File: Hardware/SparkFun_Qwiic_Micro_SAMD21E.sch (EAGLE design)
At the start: 40 parts, among them Q1 2.5A/30V/105mΩ, U1 3.3V, U2 W25Q32FV

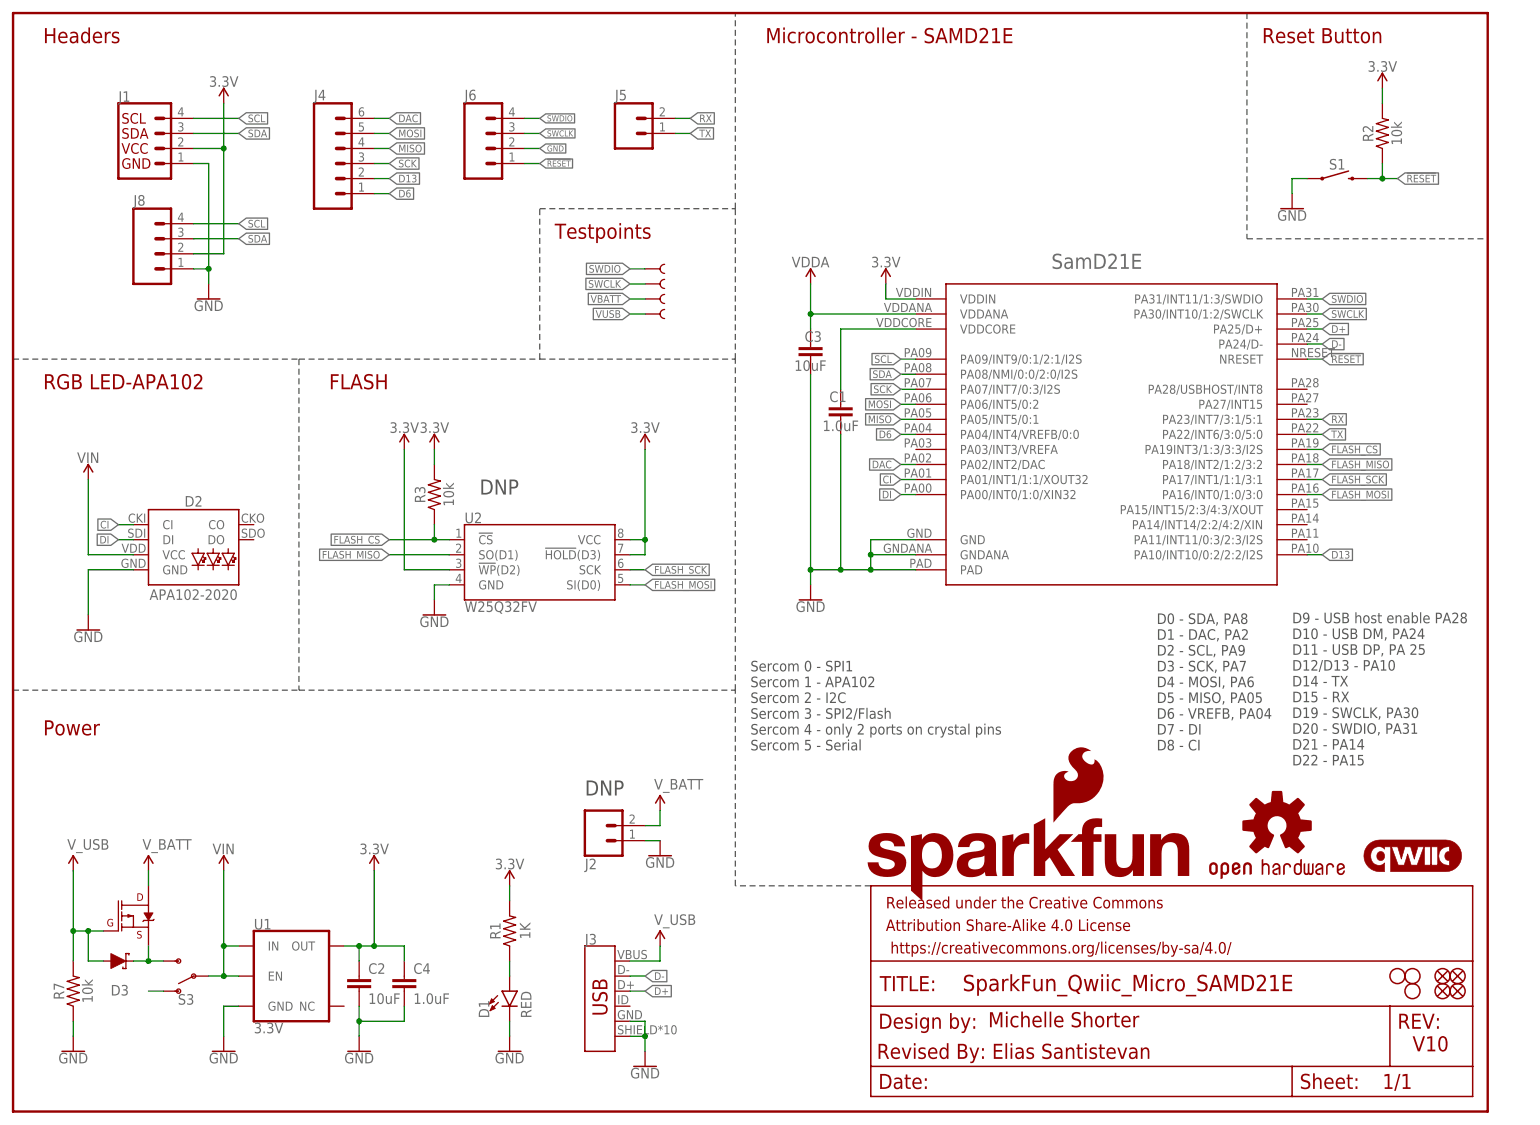
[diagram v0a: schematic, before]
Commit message: Improves all silk, replaces 0603 resistor with 0402, updates trace work for better ground pour
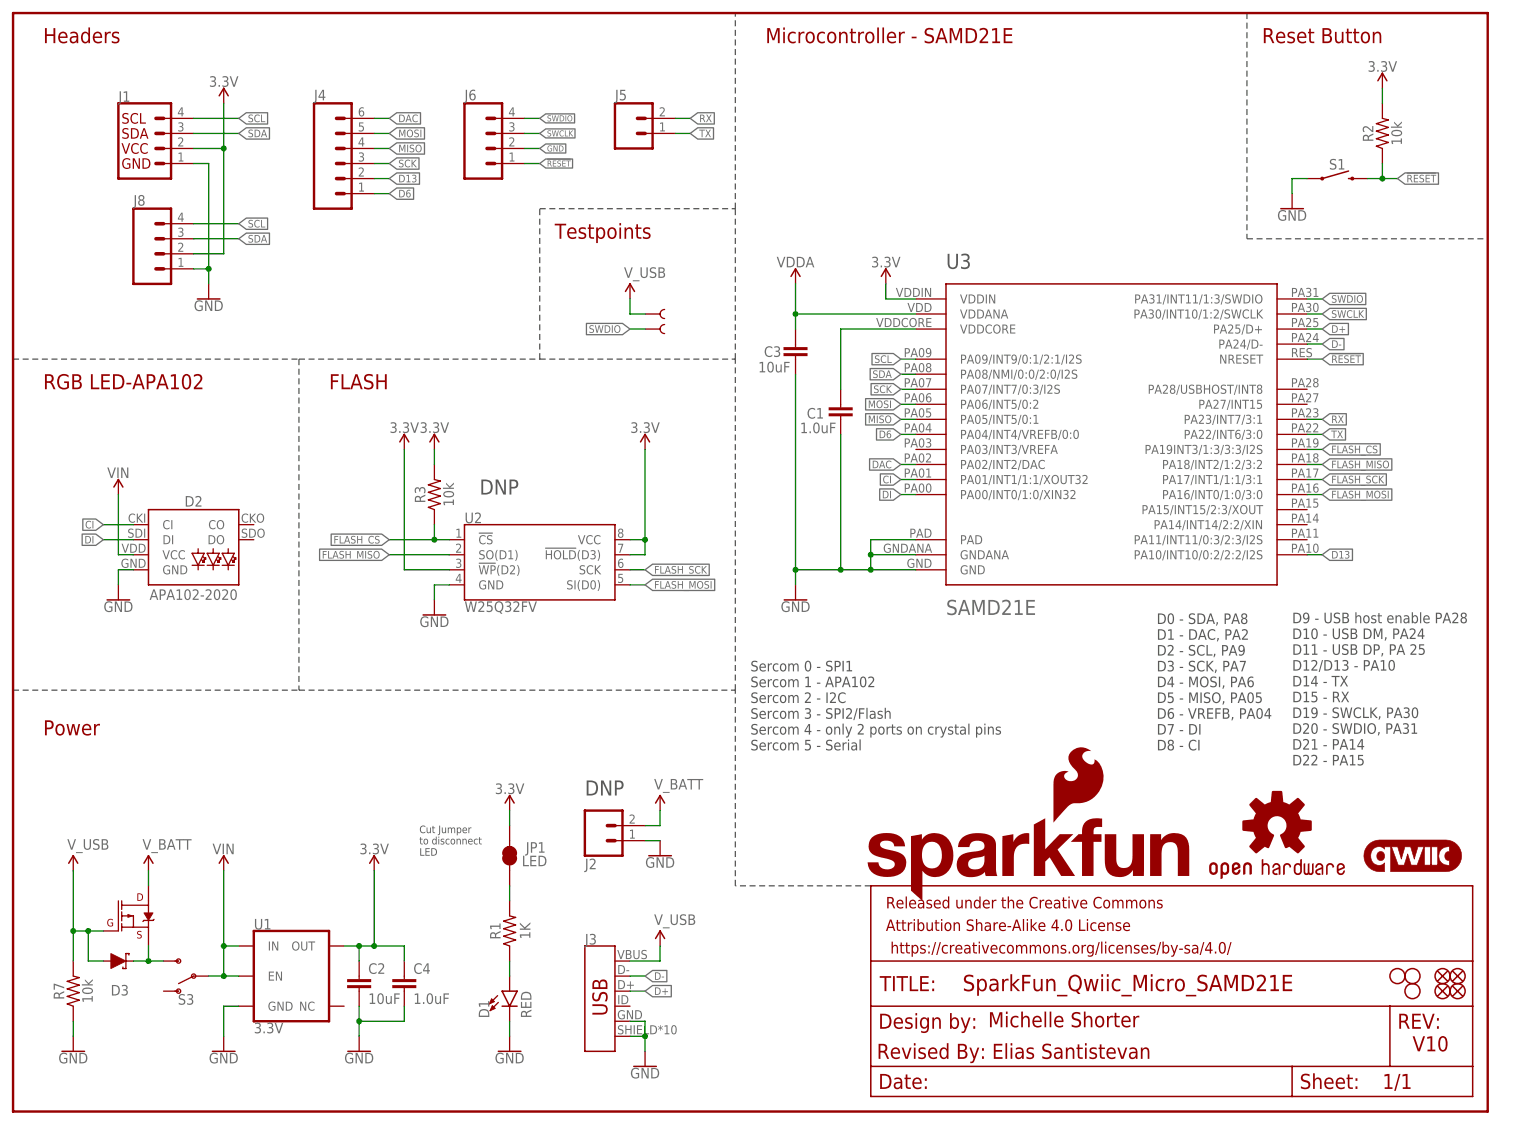
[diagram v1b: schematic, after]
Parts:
- removed SAMD21E18: SAMD32E, Test:SAMD32E
- removed TP2, TP4: TEST-POINTTP_15TH_THRU, SparkFun-Connectors:TEST-POINTTP_15TH_THRU
- added JP1: LED, SparkFun-Jumpers:JUMPER-SMT_2_NC_TRACE_SILK
- added U3: SAMD21E, Test:SAMD21E
- J6: device SparkFun-Connectors:CONN_041.27MM -> SparkFun-Connectors:CONN_041.27MM_NO_SILK
- Q1: value 2.5A/30V/105mΩ -> 3.1A/30V/105mΩ
- R7: device SparkFun-Resistors:10KOHM-0603-1/10W-1% -> SparkFun-Resistors:10KOHM-0402-1/16W-1%
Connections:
- removed net N$1 (its old number): S3.O
- removed net VBATT: Q1.D, TP2.1
- removed net VUSB: D3.A, Q1.G, R7.2, TP1.1
- new net N$2: JP1.1, R1.2
- net !RESET: now also U3.NRESET; no longer SAMD21E18.NRESET
- net 3.3V: now also JP1.2, U3.VDDIN; no longer R1.2, SAMD21E18.VDDIN
- net CI: now also U3.PA01/INT1/1:1/XOUT32; no longer SAMD21E18.PA01/INT1/1:1/XOUT32
- net D+: now also U3.PA25/D+; no longer SAMD21E18.PA25/D+
- net D-: now also U3.PA24/D-; no longer SAMD21E18.PA24/D-
- net D13: now also U3.PA10/INT10/0:2/2:2/I2S; no longer SAMD21E18.PA10/INT10/0:2/2:2/I2S
- net D6: now also U3.PA04/INT4/VREFB/0:0; no longer SAMD21E18.PA04/INT4/VREFB/0:0
- net DAC: now also U3.PA02/INT2/DAC; no longer SAMD21E18.PA02/INT2/DAC
- net DI: now also U3.PA00/INT0/1:0/XIN32; no longer SAMD21E18.PA00/INT0/1:0/XIN32
- net FLASH_CS: now also U3.PA19INT3/1:3/3:3/I2S; no longer SAMD21E18.PA19INT3/1:3/3:3/I2S
- net FLASH_MISO: now also U3.PA18/INT2/1:2/3:2; no longer SAMD21E18.PA18/INT2/1:2/3:2
- net FLASH_MOSI: now also U3.PA16/INT0/1:0/3:0; no longer SAMD21E18.PA16/INT0/1:0/3:0
- net FLASH_SCK: now also U3.PA17/INT1/1:1/3:1; no longer SAMD21E18.PA17/INT1/1:1/3:1
- net GND: now also U3.GND, U3.GNDANA, U3.PAD; no longer SAMD21E18.GND, SAMD21E18.GNDANA, SAMD21E18.PAD
- net MISO: now also U3.PA05/INT5/0:1; no longer SAMD21E18.PA05/INT5/0:1
- net MOSI: now also U3.PA06/INT5/0:2; no longer SAMD21E18.PA06/INT5/0:2
- net RX: now also U3.PA23/INT7/3:1; no longer SAMD21E18.PA23/INT7/3:1/5:1
- net SCK: now also U3.PA07/INT7/0:3/I2S; no longer SAMD21E18.PA07/INT7/0:3/I2S
- net SCL: now also U3.PA09/INT9/0:1/2:1/I2S; no longer SAMD21E18.PA09/INT9/0:1/2:1/I2S
- net SDA: now also U3.PA08/NMI/0:0/2:0/I2S; no longer SAMD21E18.PA08/NMI/0:0/2:0/I2S
- net SWCLK: now also U3.PA30/INT10/1:2/SWCLK; no longer SAMD21E18.PA30/INT10/1:2/SWCLK, TP4.1
- net SWDIO: now also U3.PA31/INT11/1:3/SWDIO; no longer SAMD21E18.PA31/INT11/1:3/SWDIO
- net TX: now also U3.PA22/INT6/3:0; no longer SAMD21E18.PA22/INT6/3:0/5:0
- net VDDA: now also U3.VDDANA; no longer SAMD21E18.VDDANA
- net VDDCORE: now also U3.VDDCORE; no longer SAMD21E18.VDDCORE
- net V_BATT: now also Q1.D
- net V_USB: now also D3.A, Q1.G, R7.2, TP1.1
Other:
- note added: "Cut Jumper to disconnect LED"
- note added: "U3"
- moved on the sheet: C3

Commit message: Moves some traces
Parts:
- LOGO3: value SFE_LOGO_FLAME.1_INCH -> SFE_LOGO_FLAME.2_INCH; device SparkFun-Aesthetics:SFE_LOGO_FLAME.1_INCH -> SparkFun-Aesthetics:SFE_LOGO_FLAME.2_INCH
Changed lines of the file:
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@@
 <part name="FRAME1" library="SparkFun-Aesthetics" deviceset="FRAME-LETTER" device=""/>
 <part name="LOGO1" library="SparkFun-Aesthetics" deviceset="OSHW-LOGO" device="S"/>
-<part name="LOGO3" library="SparkFun-Aesthetics" deviceset="SFE_LOGO_FLAME" device=".1_INCH"/>
+<part name="LOGO3" library="SparkFun-Aesthetics" deviceset="SFE_LOGO_FLAME" device=".2_INCH" value="SFE_LOGO_FLAME.2_INCH"/>
 <part name="H1" library="SparkFun-Hardware" deviceset="STAND-OFF" device=""/>
 <part name="H2" library="SparkFun-Hardware" deviceset="STAND-OFF" device=""/>

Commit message: Updates micro-controller symbol with Arduino digital pin assignments
* replaces lipo battery symbol with better one
* Re-adds battery line test ponit
* Removes info text about Arduino pin assignments
* Improves notes on SERCOM ports
* Re-numbers all parts
* Removes test library - no longer needed.
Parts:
- removed J8: (no value), SparkFun-Connectors:CONN_041X04_NO_SILK
- removed R7: 10k, SparkFun-Resistors:10KOHM-0402-1/16W-1%
- removed S3: (no value), SparkFun-Switches:SWITCH-SPDT-SMD-RIGHT-ANGLE
- added J7: (no value), SparkFun-Connectors:CONN_021X02_NO_SILK
- added R4: 10k, SparkFun-Resistors:10KOHM-0402-1/16W-1%
- added S2: MOMENTARY-SWITCH-SPST-SMD-4.6X2.8MM, SparkFun-Switches:MOMENTARY-SWITCH-SPST-SMD-4.6X2.8MM
- added TP2: TEST-POINTTP_15TH_THRU, SparkFun-Connectors:TEST-POINTTP_15TH_THRU
- C1: value 1.0uF -> 10uF; device SparkFun-Capacitors:1.0UF-0402-16V-10% -> SparkFun-Capacitors:10UF-0603-6.3V-20%
- C2: value 10uF -> 1.0uF; device SparkFun-Capacitors:10UF-0603-6.3V-20% -> SparkFun-Capacitors:1.0UF-0402-16V-10%
- D1: value RED -> 1A/23V/620mV; device SparkFun-LED:LED-RED0603 -> SparkFun-DiscreteSemi:DIODE-SCHOTTKY-BAT20J
- D3: value 1A/23V/620mV -> RED; device SparkFun-DiscreteSemi:DIODE-SCHOTTKY-BAT20J -> SparkFun-LED:LED-RED0603
- J2: device SparkFun-Connectors:CONN_02-JST-2MM-SMT -> SparkFun-Connectors:CONN_041X04_NO_SILK
- J3: device SparkFun-Connectors:USB_MICRO-B_HALF_PTH_MILL -> SparkFun-Connectors:CONN_06NO_SILK_NO_POP
- J4: device SparkFun-Connectors:CONN_06NO_SILK_NO_POP -> SparkFun-Connectors:CONN_041.27MM_NO_SILK
- J5: device SparkFun-Connectors:CONN_021X02_NO_SILK -> SparkFun-Connectors:USB_MICRO-B_HALF_PTH_MILL
- J6: device SparkFun-Connectors:CONN_041.27MM_NO_SILK -> SparkFun-Connectors:JST_2MM_MALE
- LOGO1: value OSHW-LOGOS -> SFE_LOGO_NAME.1_INCH; device SparkFun-Aesthetics:OSHW-LOGOS -> SparkFun-Aesthetics:SFE_LOGO_NAME.1_INCH
- LOGO2: value SFE_LOGO_NAME.1_INCH -> SFE_LOGO_FLAME.2_INCH; device SparkFun-Aesthetics:SFE_LOGO_NAME.1_INCH -> SparkFun-Aesthetics:SFE_LOGO_FLAME.2_INCH
- LOGO3: value SFE_LOGO_FLAME.2_INCH -> OSHW-LOGOS; device SparkFun-Aesthetics:SFE_LOGO_FLAME.2_INCH -> SparkFun-Aesthetics:OSHW-LOGOS
- R1: value 1K -> 10k; device SparkFun-Resistors:1KOHM-0402-1/16W-1% -> SparkFun-Resistors:10KOHM-0402-1/16W-1%
- R2: device SparkFun-Resistors:10KOHM-0402-1/16W-1% -> SparkFun-Resistors:10KOHM-0603-1/10W-1%
- R3: value 10k -> 1K; device SparkFun-Resistors:10KOHM-0603-1/10W-1% -> SparkFun-Resistors:1KOHM-0402-1/16W-1%
- S1: value MOMENTARY-SWITCH-SPST-SMD-4.6X2.8MM -> (none); device SparkFun-Switches:MOMENTARY-SWITCH-SPST-SMD-4.6X2.8MM -> SparkFun-Switches:SWITCH-SPDT-SMD-RIGHT-ANGLE
- U3: device Test:SAMD21E -> SparkFun-IC-Microcontroller:SAMD21E
- renumbered U$1 to LOGO4
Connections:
- net !RESET: now also J4.1, R4.1, S2.2; no longer J6.1, R2.1, S1.2
- net 3.3V: now also C1.1, J2.2, R4.2; no longer C4.1, J8.2, R3.2
- net CI: now also U3.D8_PA01/INT1/1:1/XOUT32; no longer U3.PA01/INT1/1:1/XOUT32
- net D+: now also J5.D+, U3.PA25/D+_D11; no longer J3.D+, U3.PA25/D+
- net D-: now also J5.D-, U3.PA24/D-_D10; no longer J3.D-, U3.PA24/D-
- net D13: now also J3.2, U3.PA10/INT10/0:2/2:2/I2S_D13; no longer J4.2, U3.PA10/INT10/0:2/2:2/I2S
- net D6: now also J3.1, U3.D6_PA04/INT4/VREFB/0:0; no longer J4.1, U3.PA04/INT4/VREFB/0:0
- net DAC: now also J3.6, U3.D1_PA02/INT2/DAC; no longer J4.6, U3.PA02/INT2/DAC
- net DI: now also U3.D7_PA00/INT0/1:0/XIN32; no longer U3.PA00/INT0/1:0/XIN32
- net FLASH_CS: now also R2.1; no longer R3.1
- net GND: now also C1.2, C4.1, D3.C, J2.1, J4.2, J5.GND, J5.SHIELD, J6.-, R1.1, S2.1; no longer C1.1, C4.2, D1.C, J2.2, J3.GND, J3.SHIELD, J6.2, J8.1, R7.1, S1.1
- net MISO: now also J3.4, U3.D5_PA05/INT5/0:1; no longer J4.4, U3.PA05/INT5/0:1
- net MOSI: now also J3.5, U3.D4_PA06/INT5/0:2; no longer J4.5, U3.PA06/INT5/0:2
- net N$1: now also D3.A, R3.1; no longer D1.A, R1.1
- net N$2: now also R3.2; no longer R1.2
- net RX: now also J7.2, U3.PA23/INT7/3:1_D15; no longer J5.2, U3.PA23/INT7/3:1
- net SCK: now also J3.3, U3.D3_PA07/INT7/0:3/I2S; no longer J4.3, U3.PA07/INT7/0:3/I2S
- net SCL: now also J2.4, U3.D2_PA09/INT9/0:1/2:1/I2S; no longer J8.4, U3.PA09/INT9/0:1/2:1/I2S
- net SDA: now also J2.3, U3.D0_PA08/NMI/0:0/2:0/I2S; no longer J8.3, U3.PA08/NMI/0:0/2:0/I2S
- net SWCLK: now also J4.3, U3.PA30/INT10/1:2/SWCLK_D19; no longer J6.3, U3.PA30/INT10/1:2/SWCLK
- net SWDIO: now also J4.4, U3.PA31/INT11/1:3/SWDIO_D20; no longer J6.4, U3.PA31/INT11/1:3/SWDIO
- net TX: now also J7.1, U3.PA22/INT6/3:0_D14; no longer J5.1, U3.PA22/INT6/3:0
- net VDDCORE: now also C4.2; no longer C1.2
- net VIN: now also S1.P; no longer S3.P
- net VIN1: now also D1.C, S1.S; no longer D3.C, S3.S
- net V_BATT: now also J6.+, TP2.1; no longer J2.1
- net V_USB: now also D1.A, J5.VBUS, R1.2; no longer D3.A, J3.VBUS, R7.2
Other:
- note added: "Notes on SERCOM Ports"
- note removed: "D0 - SDA, PA8 D1 - DAC, PA2 D2 - SCL, PA9 D3 - SCK, PA7 D4 - MOSI, PA6 D5 - MISO, PA05 D6 - VREFB, PA04 D7 - DI D8 - CI"
- note removed: "D9 - USB host enable PA28 D10 - USB DM, PA24 D11 - USB DP, PA 25 D12/D13 - PA10 D14 - TX D15 - RX D19 - SWCLK, PA30 D20 - SWDIO, PA31 D21 - PA14 D22 - PA15"
- moved on the sheet: C1, C2, C3, C4, R1, R2, R3
